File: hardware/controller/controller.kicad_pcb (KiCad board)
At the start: 2 copper layers, 150 x 68 mm, 194 parts, among them J1 Conn_01x05, J2 Conn_01x03, J3 Conn_01x04, J4 USB_B_Micro, J5 Conn_01x03, J6 Conn_01x02, Q1 MMBT2222A 1P, Q2 AO3400A, SW1 ILS_TA180_50, SW10 SW_Push, SW11 SW_SPDT, SW2 ILS_TA180_50, SW3 ILS_TA180_50, SW4 ILS_TA180_50, SW5 ILS_TA180_50, SW6 ILS_TA180_50, SW7 ILS_TA180_50, SW8 ILS_TA180_50, SW9 ILS_TA180_50, U1 WS2811, U10 CH340X, U2 FM24CL16B, U3 WS2811, U4 WS2811, U5 HT75xx-1-SOT89, U6 RFM69CW-915MHZ, U7 TP4056, U8 STM32G070CBTx, U9 ISL29125

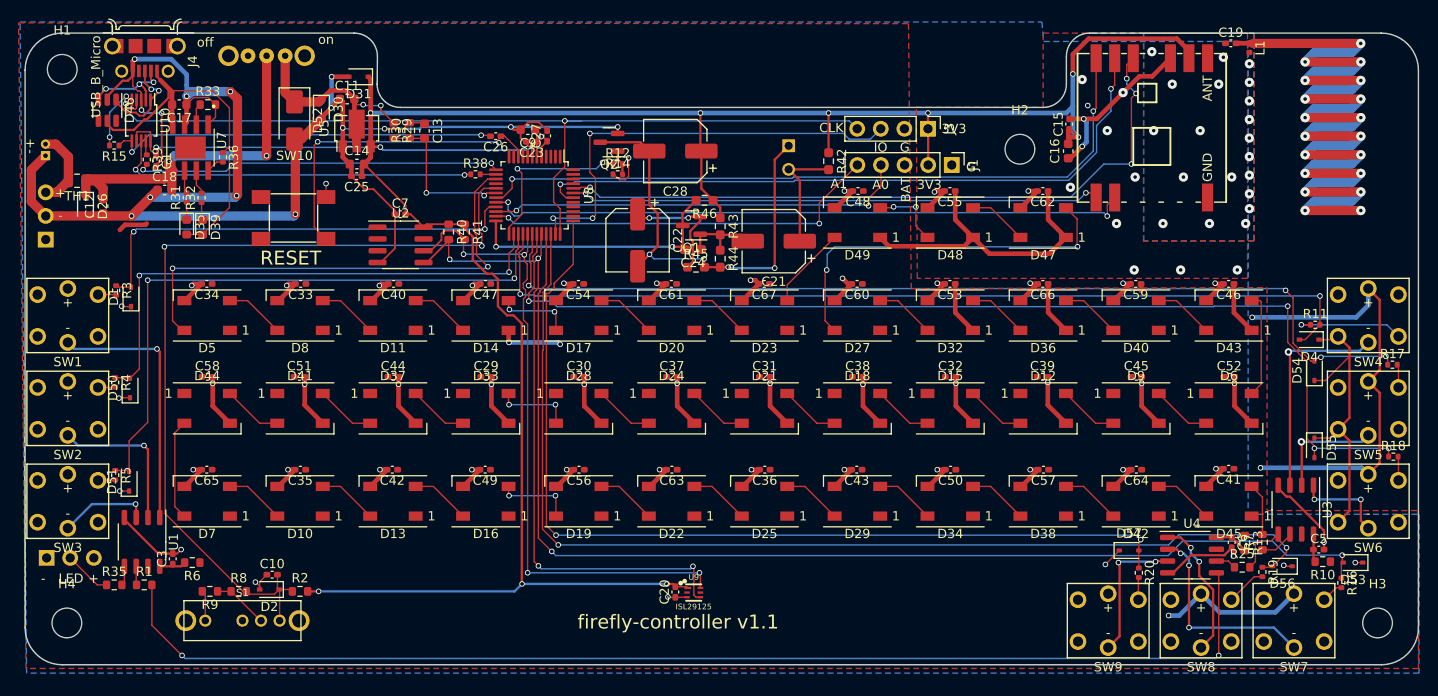
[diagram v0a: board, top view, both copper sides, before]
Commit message: Cost optimizations for controller v1.1
This consolidates some of the resistors values to reduce the number of
BOM line items.

Change-Id: Ia3d1077ce7e82b015c1ec4700b90b76e07124758
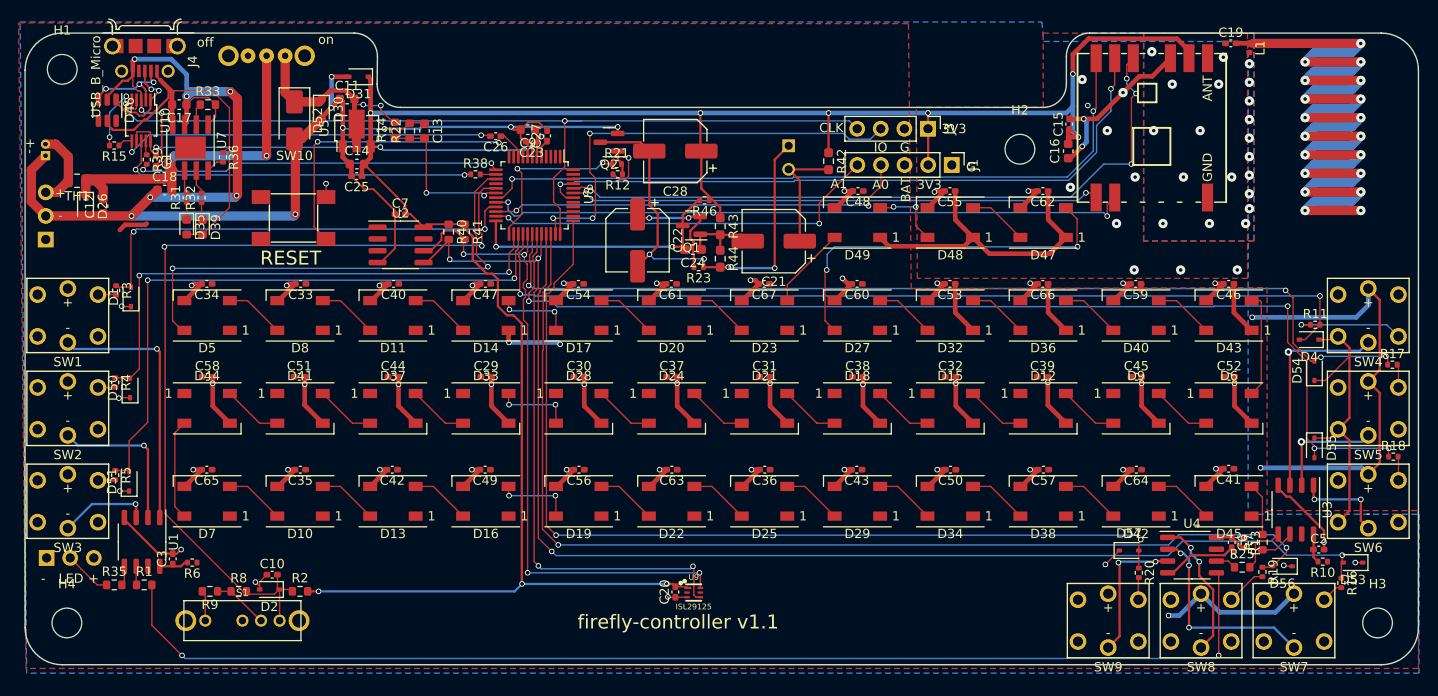
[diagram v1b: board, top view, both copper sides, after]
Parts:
- removed R29: 62k, Resistor_SMD:R_0603_1608Metric
- removed R30: 180k, Resistor_SMD:R_0603_1608Metric
- removed R45: 220, Resistor_SMD:R_0603_1608Metric_Pad0.98x0.95mm_HandSolder
- added R21: 100, Resistor_SMD:R_0402_1005Metric, F.Cu at (94.1, 103.7)
- added R22: 680k, Resistor_SMD:R_0603_1608Metric, F.Cu at (71.8, 100.1)
- added R23: 220, Resistor_SMD:R_0402_1005Metric, F.Cu at (102.9, 114.8)
- R10, R13, R6: footprint Resistor_SMD:R_0603_1608Metric -> Resistor_SMD:R_0402_1005Metric
- R12: value 220 -> 4k7
- R14: value 10k -> 240k; footprint Resistor_SMD:R_0402_1005Metric -> Resistor_SMD:R_0603_1608Metric
- R46: footprint Resistor_SMD:R_0603_1608Metric_Pad0.98x0.95mm_HandSolder -> Resistor_SMD:R_0402_1005Metric
- moved R14 24.5 mm to (70.2, 100.0), turned to 90 degrees
- moved R12 1.10 mm to (94.2, 104.8), turned to 180 degrees
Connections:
- R12 pad 1: /MIC_ENABLE -> Net-(Q2-G)
- R12 pad 2: Net-(Q2-G) -> GND
- R14 pad 1: GND -> /VBATT_DIV
- R14 pad 2: Net-(Q2-G) -> +BATT

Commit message: Controller v1.1 updates:
- Move crowbar diode before the switch
- Change to in-stock TVS diodes

Change-Id: I54c2ed7b3562a7853553227b0bcbf77bde420927
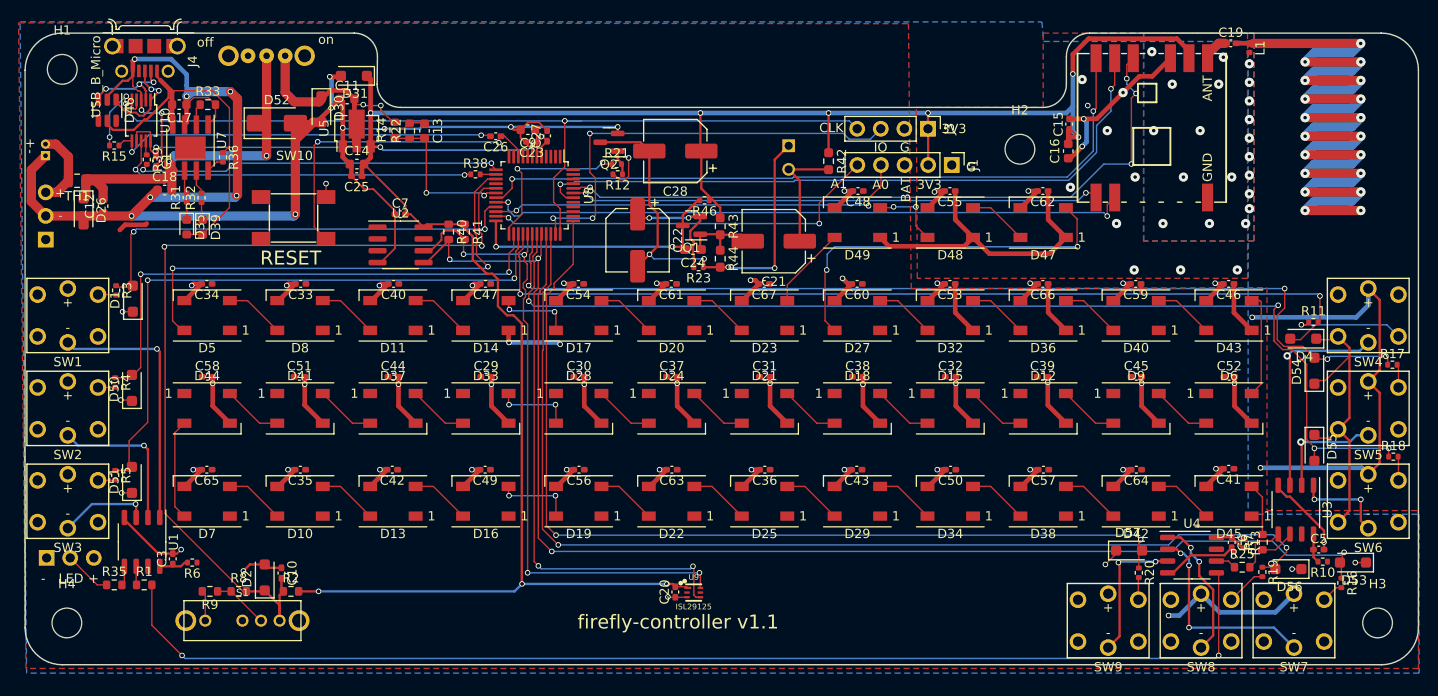
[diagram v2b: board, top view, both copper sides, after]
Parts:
- D1, D2, D26, D30, D31, D4, D50, D51, D53, D54, D55, D56, D57: footprint Diode_SMD:D_SOD-323 -> Diode_SMD:D_SOD-123F
- J4: footprint homebrew:FRAMATOME_10118194-0001LF_fixed_bridges -> Homebrew:FRAMATOME_10118194-0001LF_fixed_bridges
- S1: footprint snapeda:OS102011MS8QP1 -> Homebrew:OS102011MS8QP1
- U6: footprint homebrew:RFM69CW-minimalpads -> Homebrew:RFM69CW-minimalpads
- moved D52 1.92 mm to (57.5, 99.3), turned to 0 degrees
- moved D2 1.39 mm to (56.2, 148.2), turned to 90 degrees
- moved C10 1.01 mm to (58.0, 147.7), turned to -90 degrees
- moved R2 0.98 mm to (59.0, 149.7)
- moved D56 0.72 mm to (166.4, 147.3)
- moved D4 0.66 mm to (168.0, 122.5)
- moved D26 0.59 mm to (36.7, 108.8)
- moved D31 0.51 mm to (65.8, 94.2)
- moved R11 0.36 mm to (169.1, 120.7)
- moved D51 0.34 mm to (41.9, 137.7)
- moved D1 0.28 mm to (42.0, 118.2)
- moved D50 0.20 mm to (41.9, 127.8)
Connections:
- D52 pad 1: +BATT -> /BATT_DIRECT
- U6 pad 1: Net-(C19-Pad1) -> Net-(U6-ANT)
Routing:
- net GND: track 440.2 -> 443.3 mm
- net Net-(U6-ANT): track 0.00 -> 2.83 mm
- net /SW_RIGHT2: track 105.5 -> 107.0 mm
- net VCC: track 288.8 -> 289.7 mm
- net /SW_MODE: track 92.8 -> 93.4 mm

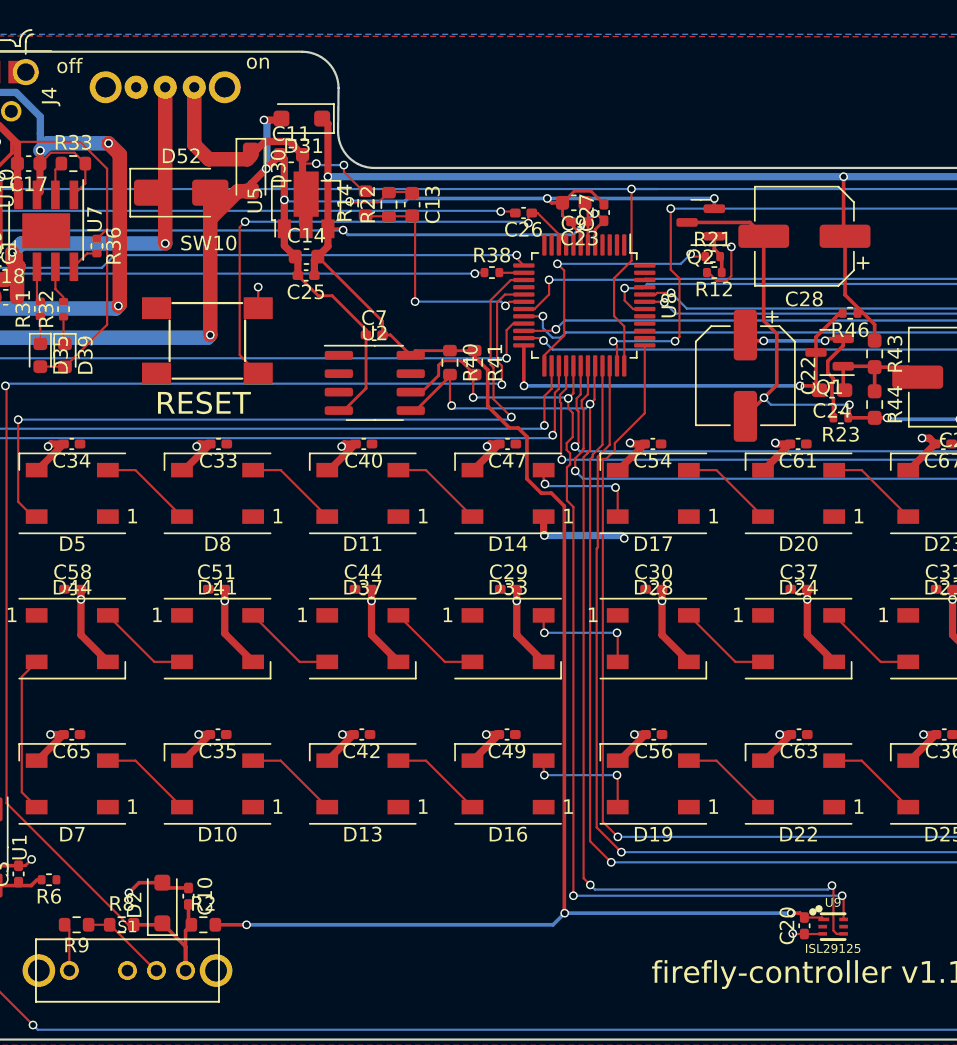
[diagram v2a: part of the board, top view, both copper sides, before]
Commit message: Update controller PCB v1.1:
- Switch to in-stock light sensor
- Move power switch to top of board, so it's populated by JLC

Change-Id: I8973979a1cd224c9d926090501cf37b5c34c39ea
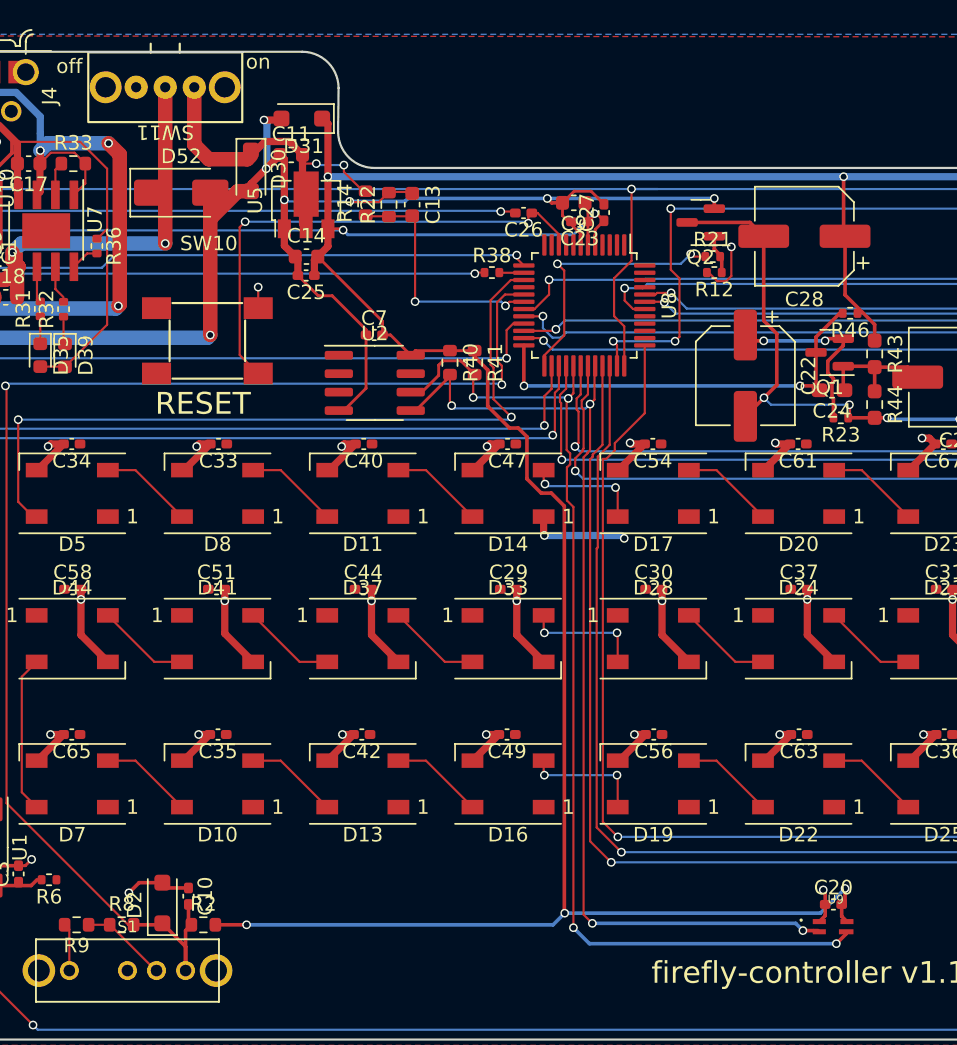
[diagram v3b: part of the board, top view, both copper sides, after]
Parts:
- SW11: moved to F.Cu
- U9: value ISL29125 -> VEML6040; footprint Sparkfun_Silicon_Standard:ODFN-6 -> Homebrew:VISHAY_VEML6040_1.25X2X1
- moved C20 2.48 mm to (102.4, 148.3), turned to 0 degrees
- turned SW11 to 180 degrees
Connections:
- SW11 pad 1: unconnected-(SW11-A-Pad1) -> +BATT
- SW11 pad 3: +BATT -> unconnected-(SW11-C-Pad3)
- U9 pad 1: VCC -> GND
- U9 pad 2: (no net) -> /SDA
- U9 pad 3: GND -> /SCL
- U9 pad 4: /SDA -> VCC
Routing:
- net VCC: track 289.7 -> 294.3 mm
- net /SDA: track 72.3 -> 69.9 mm
- net /SCL: track 70.8 -> 72.3 mm

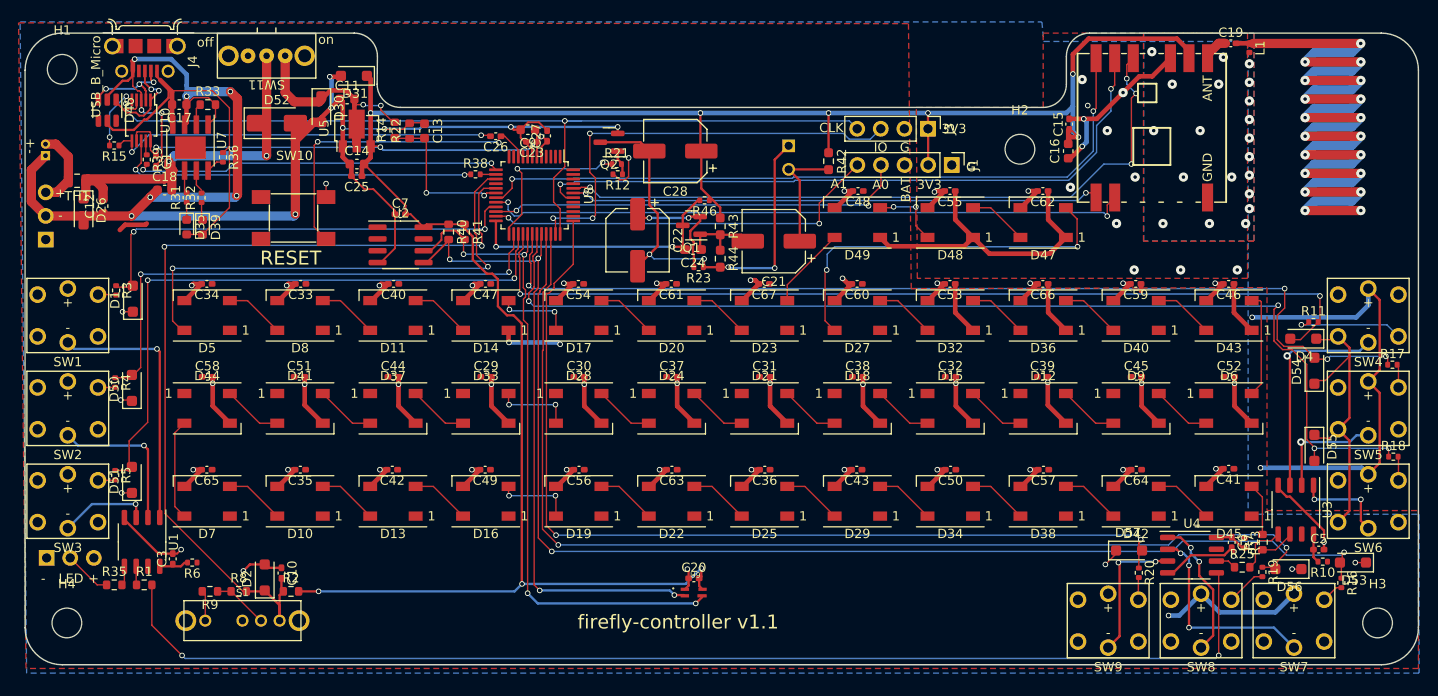
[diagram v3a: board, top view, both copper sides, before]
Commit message: Update the controller 3d model for v1.2
Change-Id: Id3ad5075ae00748a24c8b9b0fe9f947010f8c823
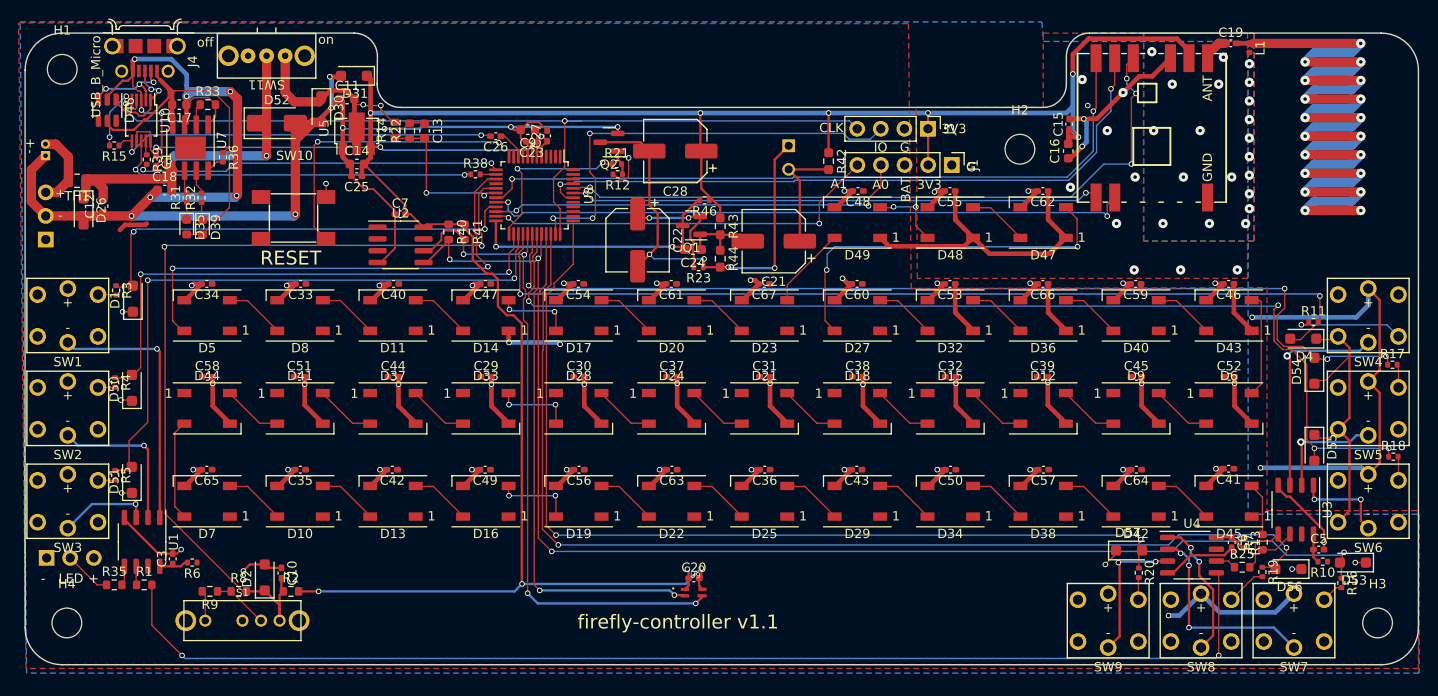
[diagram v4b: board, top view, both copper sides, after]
